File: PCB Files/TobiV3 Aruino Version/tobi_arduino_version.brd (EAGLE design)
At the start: 103 x 74 mm, 45 parts

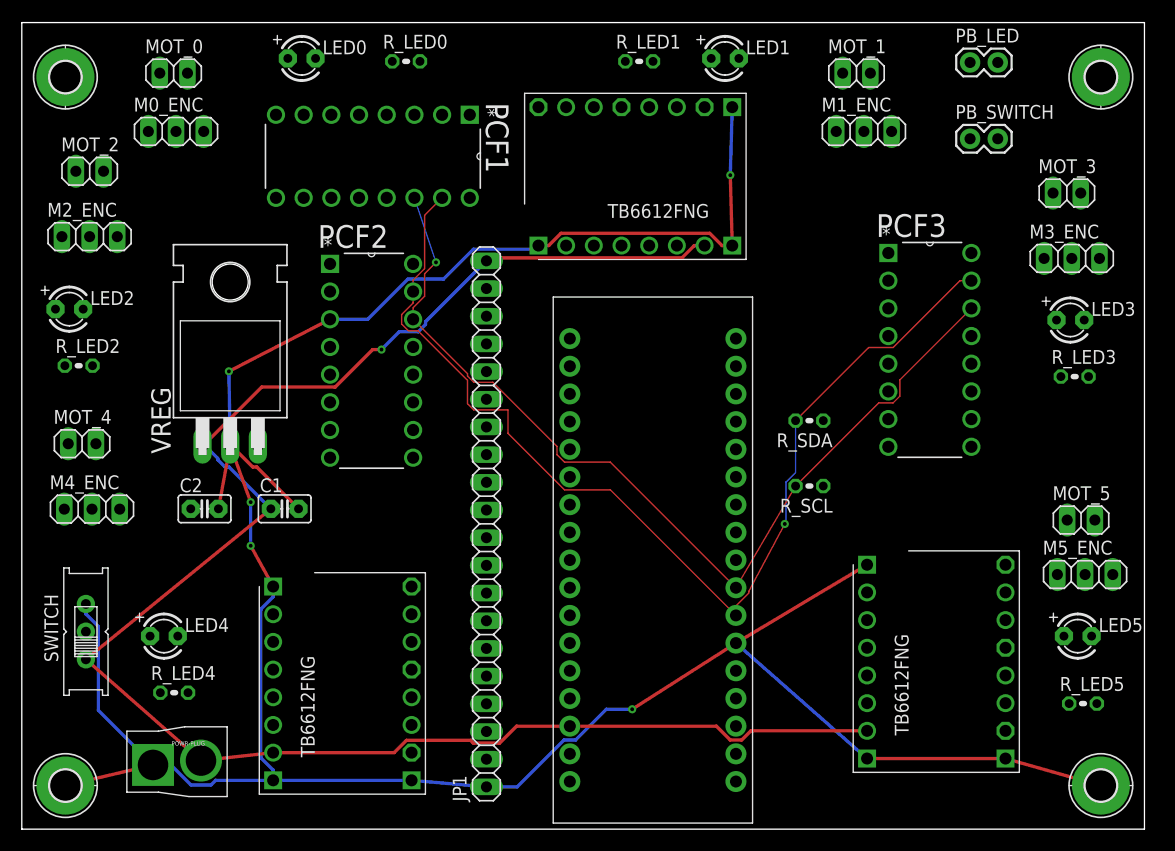
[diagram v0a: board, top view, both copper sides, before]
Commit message: route heavy traces for motor leads
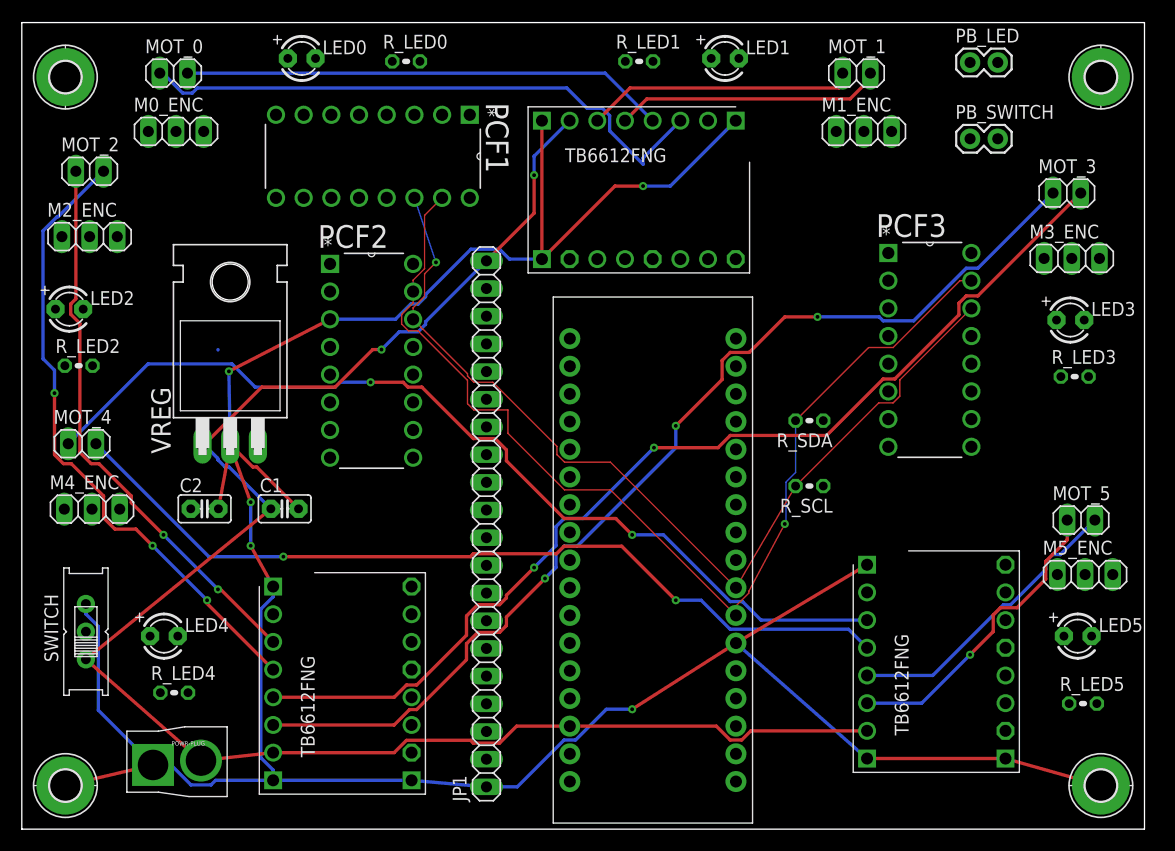
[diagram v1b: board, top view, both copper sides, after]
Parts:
- moved DRIVER1 24.4 mm to (43.5, 72.3), turned to 270 degrees
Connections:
- net M4_B: no longer DRIVER3.BO2
- net M5_B: now also DRIVER3.BO2
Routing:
- net M3_A: track 0.00 -> 96.3 mm, vias 0 -> 3
- net M3_B: track 0.00 -> 96.1 mm, vias 0 -> 2
- net M4_A: track 0.00 -> 87.0 mm, vias 0 -> 2
- net M4_B: track 0.00 -> 79.3 mm, vias 0 -> 2
- net M2_B: track 0.00 -> 58.4 mm, vias 0 -> 3
- net M0_A: track 0.00 -> 54.4 mm
- net M2_A: track 0.00 -> 51.6 mm, vias 0 -> 2
- net M0_B: track 0.00 -> 44.5 mm
- net M5_A: track 0.00 -> 28.2 mm, vias 0 -> 1
- net M5_B: track 0.00 -> 27.2 mm
- net M1_A: track 0.00 -> 24.9 mm
- net M1_B: track 0.00 -> 24.6 mm
- net GND: track 254.4 -> 259.4 mm
- net V_MOT: track 163.6 -> 159.4 mm, vias 1 -> 2

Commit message: autoroute the rest of the board
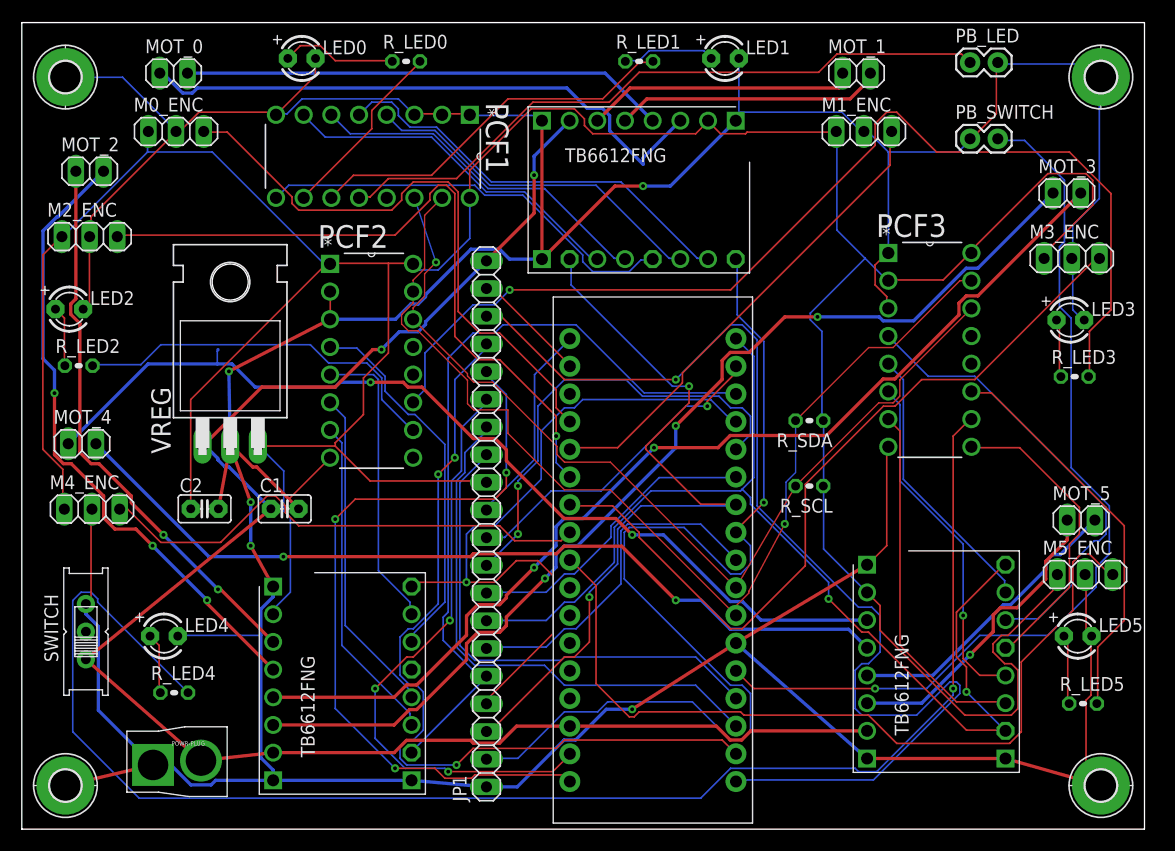
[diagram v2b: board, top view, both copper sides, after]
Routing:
- net VCC: track 0.00 -> 325.6 mm
- net GND: track 259.4 -> 478.9 mm
- net LED4: track 0.00 -> 140.5 mm, vias 0 -> 1
- net MOSI: track 0.00 -> 106.3 mm, vias 0 -> 1
- net LED3: track 0.00 -> 99.0 mm, vias 0 -> 1
- net M5_PWM: track 0.00 -> 99.0 mm, vias 0 -> 2
- net M0_PWM: track 0.00 -> 96.4 mm, vias 0 -> 1
- net RESET: track 0.00 -> 85.2 mm, vias 0 -> 1
- net M5_ENC: track 0.00 -> 76.7 mm
- net SS: track 0.00 -> 76.6 mm, vias 0 -> 3
- net M3_ENC: track 0.00 -> 72.1 mm
- net M3_PWM: track 0.00 -> 71.9 mm
- net M1_PWM: track 0.00 -> 71.0 mm, vias 0 -> 2
- net SCK: track 0.00 -> 70.3 mm, vias 0 -> 3
- net M2_PWM: track 0.00 -> 66.6 mm, vias 0 -> 1
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
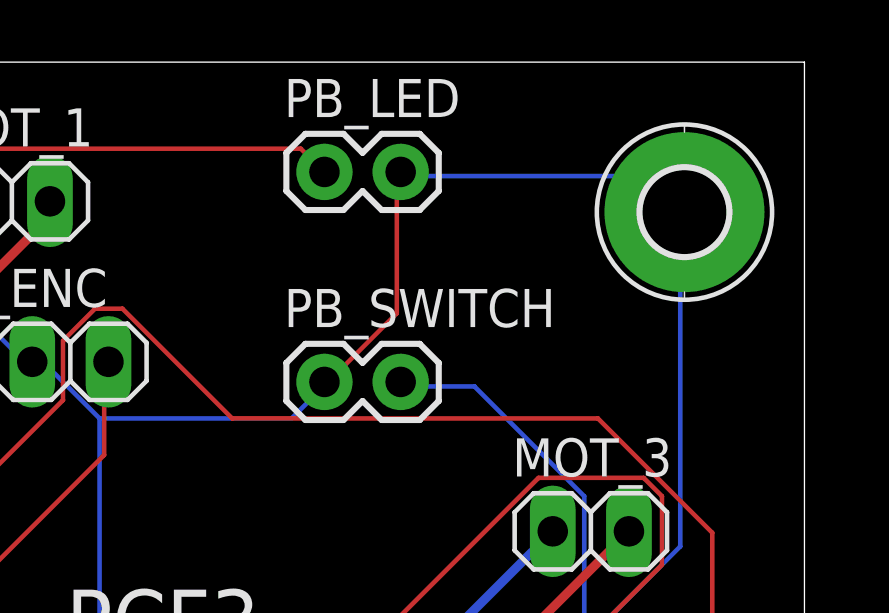
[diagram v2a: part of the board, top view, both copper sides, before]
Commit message: fix silkscreen on pushbutton LED
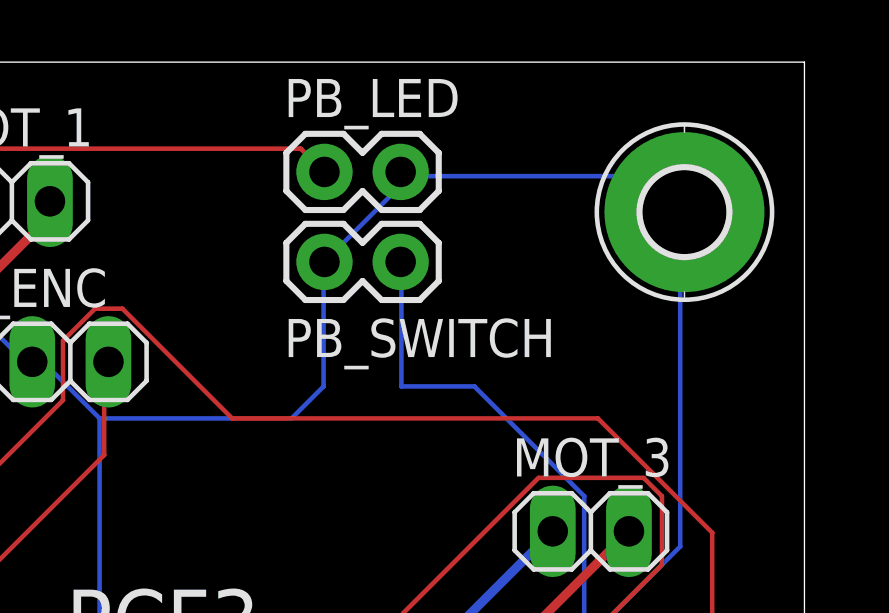
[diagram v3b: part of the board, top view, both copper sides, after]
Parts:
- moved PB_SWITCH 4.00 mm to (84.0, 73.3)
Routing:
- net RESET: track 85.2 -> 89.3 mm
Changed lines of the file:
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@@
 <element name="LED4" library="adafruit" package="LED3MM" value="" x="10.04" y="23.71"/>
 <element name="LED5" library="adafruit" package="LED3MM" value="" x="93.88" y="23.71"/>
-<element name="PB_LED" library="SparkFun-Connectors" package="1X02" value="M02PTH" x="84" y="76.34"/>
-<element name="PB_SWITCH" library="SparkFun-Connectors" package="1X02" value="M02PTH" x="84" y="69.34"/>
+<element name="PB_LED" library="SparkFun-Connectors" package="1X02" value="M02PTH" x="84" y="76.34" smashed="yes">
+<attribute name="NAME" x="82.6538" y="78.1688" size="1.27" layer="25" ratio="10"/>
+</element>
+<element name="PB_SWITCH" library="SparkFun-Connectors" package="1X02" value="M02PTH" x="84" y="73.34" smashed="yes">
+<attribute name="NAME" x="82.6538" y="70.1688" size="1.27" layer="25" ratio="10"/>
+</element>
 <element name="PCF1" library="Texas Instruments_By_element14_Batch_1" package="DIP254P762X508-16" value="PCF8574AN" x="20.32" y="63.92" rot="R270">
 <attribute name="MPN" value="PCF8574AN" x="20.32" y="63.92" size="1.778" layer="27" rot="R270" display="off"/>
@@
 <wire x1="76.5048" y1="68.1228" x2="74.676" y2="69.9516" width="0.1524" layer="16"/>
 <wire x1="82.9056" y1="68.1228" x2="76.5048" y2="68.1228" width="0.1524" layer="16"/>
-<wire x1="83.9724" y1="69.1896" x2="82.9056" y2="68.1228" width="0.1524" layer="16"/>
+<wire x1="82.9056" y1="68.1228" x2="83.9724" y2="69.1896" width="0.1524" layer="16"/>
 <wire x1="74.3712" y1="69.9516" x2="74.26" y2="70.01" width="0.1524" layer="16"/>
-<wire x1="83.9724" y1="69.1896" x2="84" y2="69.34" width="0.1524" layer="16"/>
-<wire x1="86.4108" y1="71.628" x2="86.4108" y2="76.2" width="0.1524" layer="1"/>
-<wire x1="84.1248" y1="69.342" x2="86.4108" y2="71.628" width="0.1524" layer="1"/>
 <wire x1="86.4108" y1="76.2" x2="86.54" y2="76.34" width="0.1524" layer="1"/>
-<wire x1="84.1248" y1="69.342" x2="84" y2="69.34" width="0.1524" layer="1"/>
 <wire x1="76.5048" y1="68.1228" x2="76.5048" y2="58.9788" width="0.1524" layer="16"/>
 <wire x1="76.5048" y1="58.9788" x2="76.5" y2="58.86" width="0.1524" layer="16"/>
@@
 <wire x1="20.4216" y1="71.628" x2="20.32" y2="71.54" width="0.1524" layer="16"/>
 <wire x1="32.9184" y1="71.628" x2="33.02" y2="71.54" width="0.1524" layer="16"/>
+<wire x1="83.9724" y1="69.1896" x2="83.9724" y2="73.3124" width="0.1524" layer="16"/>
+<wire x1="83.9724" y1="73.3124" x2="84" y2="73.34" width="0.1524" layer="16"/>
+<wire x1="84" y1="73.34" x2="86.5632" y2="75.9032" width="0.1524" layer="16"/>
+<wire x1="86.5632" y1="75.9032" x2="86.5632" y2="76.2" width="0.1524" layer="16"/>
 </signal>
 <signal name="M4_M5_EN">
@@
 <wire x1="64.1604" y1="18.8976" x2="75.2856" y2="18.8976" width="0.1524" layer="1"/>
 <wire x1="62.6364" y1="20.4216" x2="64.1604" y2="18.8976" width="0.1524" layer="1"/>
-<wire x1="86.5632" y1="69.1896" x2="86.54" y2="69.34" width="0.1524" layer="16"/>
 <wire x1="62.6364" y1="20.4216" x2="62.52" y2="20.53" width="0.1524" layer="1"/>
 <via x="75.2856" y="18.8976" extent="1-16" drill="0.35"/>
+<wire x1="86.5632" y1="69.1896" x2="86.5632" y2="73.3168" width="0.1524" layer="16"/>
+<wire x1="86.5632" y1="73.3168" x2="86.54" y2="73.34" width="0.1524" layer="16"/>
 </signal>
 <signal name="V_IN_1">

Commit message: rip up main board and try again...
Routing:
- net GND: track 478.9 -> 0.00 mm, vias 5 -> 0
- net VCC: track 325.6 -> 0.09 mm
- net V_MOT: track 159.4 -> 0.38 mm, vias 2 -> 0
- net LED4: track 140.5 -> 0.00 mm, vias 1 -> 0
- net MOSI: track 106.3 -> 0.00 mm, vias 1 -> 0
- net LED3: track 99.0 -> 0.00 mm, vias 1 -> 0
- net M5_PWM: track 99.0 -> 0.00 mm, vias 2 -> 0
- net SDA: track 98.4 -> 0.00 mm, vias 1 -> 0
- net M0_PWM: track 96.4 -> 0.00 mm, vias 1 -> 0
- net M3_A: track 96.3 -> 0.00 mm, vias 3 -> 0
- net M3_B: track 96.1 -> 0.00 mm, vias 2 -> 0
- net RESET: track 89.3 -> 0.00 mm, vias 1 -> 0
- net M4_A: track 88.3 -> 0.00 mm, vias 2 -> 0
- net SCL: track 87.3 -> 0.00 mm, vias 1 -> 0
- net M4_B: track 79.3 -> 0.00 mm, vias 2 -> 0
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
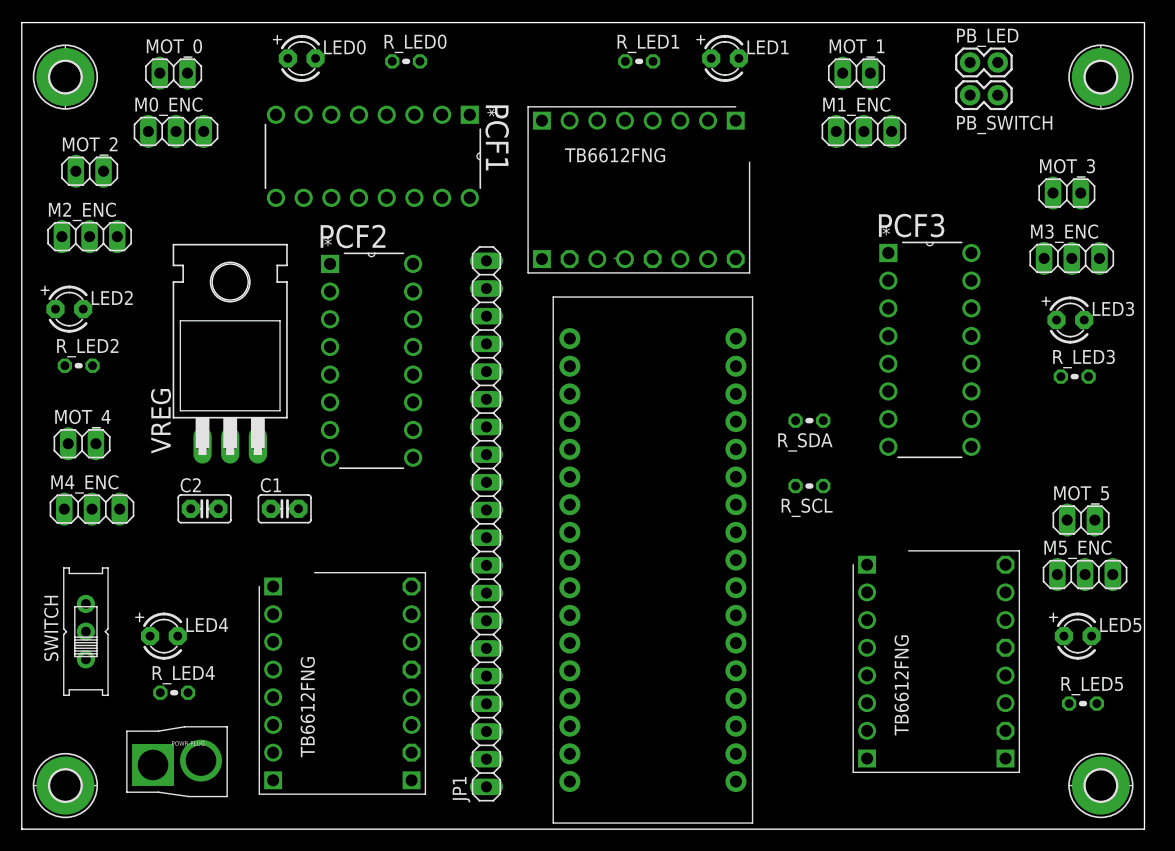
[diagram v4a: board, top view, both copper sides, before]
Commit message: add ground plane
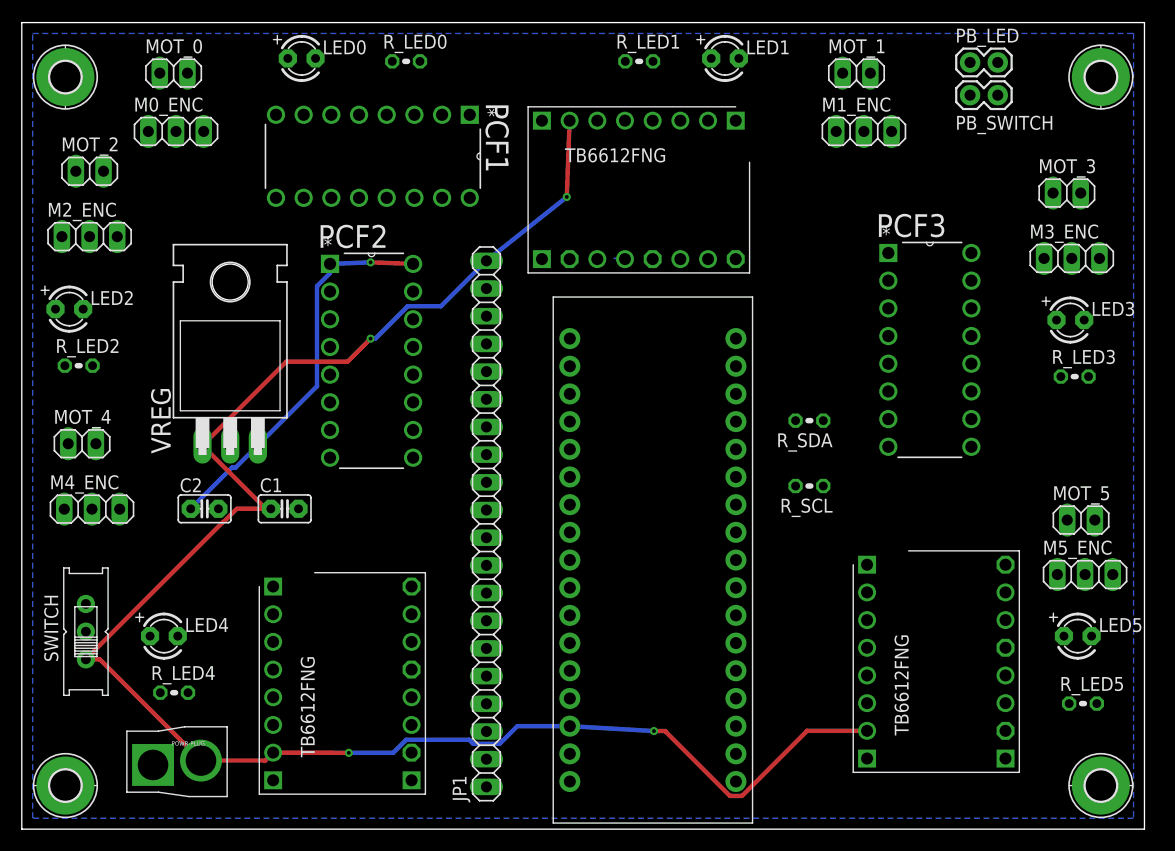
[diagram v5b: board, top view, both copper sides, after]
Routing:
- net V_MOT: track 0.38 -> 163.3 mm, vias 0 -> 4
- net VCC: track 0.09 -> 35.7 mm, vias 0 -> 1
- added copper zone on layer 16, net GND

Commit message: add thick traces for battery voltage, motor voltage, sda, scl
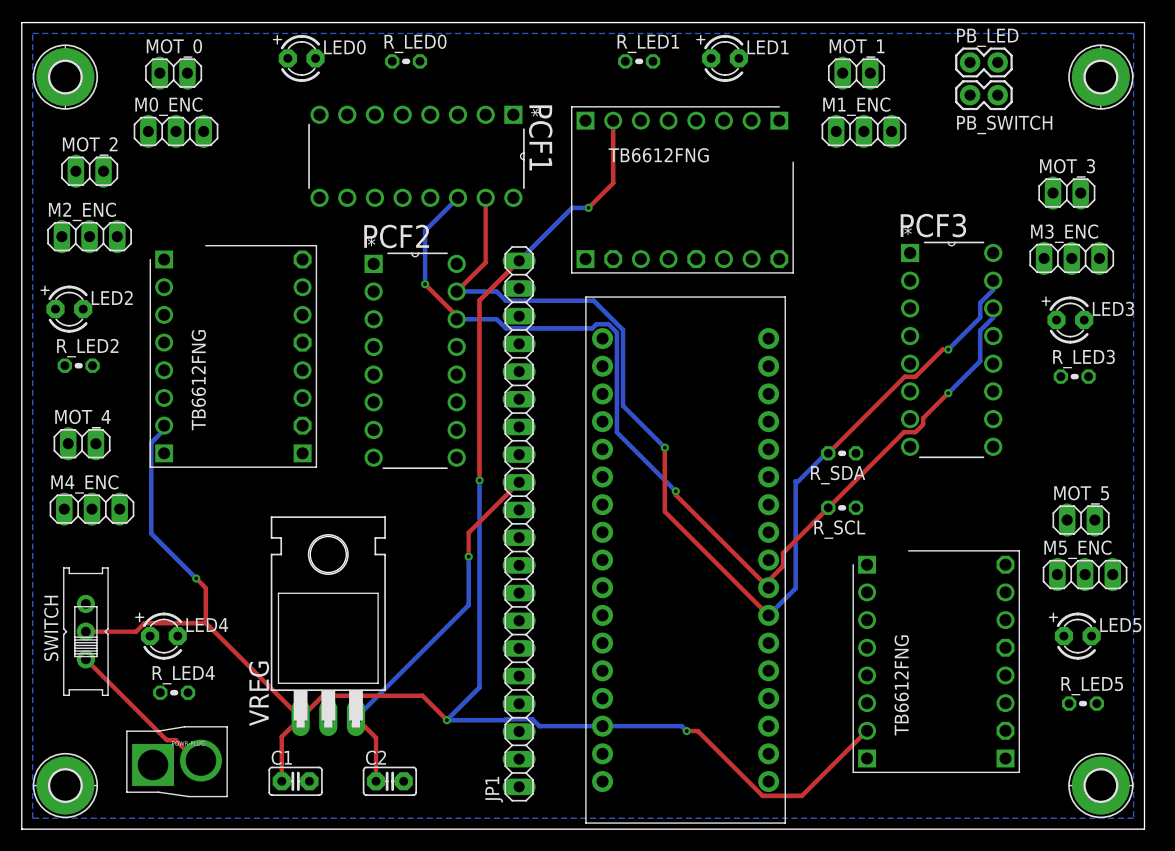
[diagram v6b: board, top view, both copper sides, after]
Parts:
- moved DRIVER2 31.6 mm to (8.79, 39.2)
- moved C2 30.2 mm to (30.8, 10.4)
- moved VREG 26.6 mm to (25.1, 26.4)
- moved C1 25.0 mm to (22.1, 10.4)
- moved R_SDA 4.24 mm to (72.3, 40.5)
- moved DRIVER1 4.00 mm to (47.5, 72.3)
- moved PCF1 4.00 mm to (24.3, 63.9)
- moved PCF2 4.00 mm to (36.9, 40.1)
- moved R_SCL 3.61 mm to (72.3, 35.5)
- moved ARDUINOMICRO 3.00 mm to (57.9, 30.7)
- moved JP1 3.00 mm to (42.6, 34.0)
- moved PCF3 2.00 mm to (86.1, 41.1)
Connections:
- removed net V_IN_1: SWITCH.P
- new net V_BATT: POWR-PLUG.POW, SWITCH.O
- net V_MOT: now also SWITCH.P; no longer POWR-PLUG.POW, SWITCH.O
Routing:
- net SDA: track 0.00 -> 98.5 mm, vias 0 -> 2
- net SCL: track 0.00 -> 93.1 mm, vias 0 -> 3
- net V_BATT: track 0.00 -> 14.4 mm
- net V_MOT: track 163.3 -> 172.2 mm, vias 4 -> 5
- net VCC: track 35.7 -> 34.4 mm
- net M1_IN1: track 1.01 -> 0.00 mm
- net M1_IN2: track 0.59 -> 0.00 mm
